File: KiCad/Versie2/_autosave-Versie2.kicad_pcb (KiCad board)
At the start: 2 copper layers, 95 parts, among them IC1 AP9221SA-CC-HAC-7, IC2 ISL91107IRTNZ-T7A, J1 Micro_SD_Card, J10 Screw_Terminal_01x02, J11 Screw_Terminal_01x02, J12 Screw_Terminal_01x03, J2 USB_C_Receptacle_USB3.0, J3 JTAG, J4 Programmer, J5 Conn_01x06_Male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

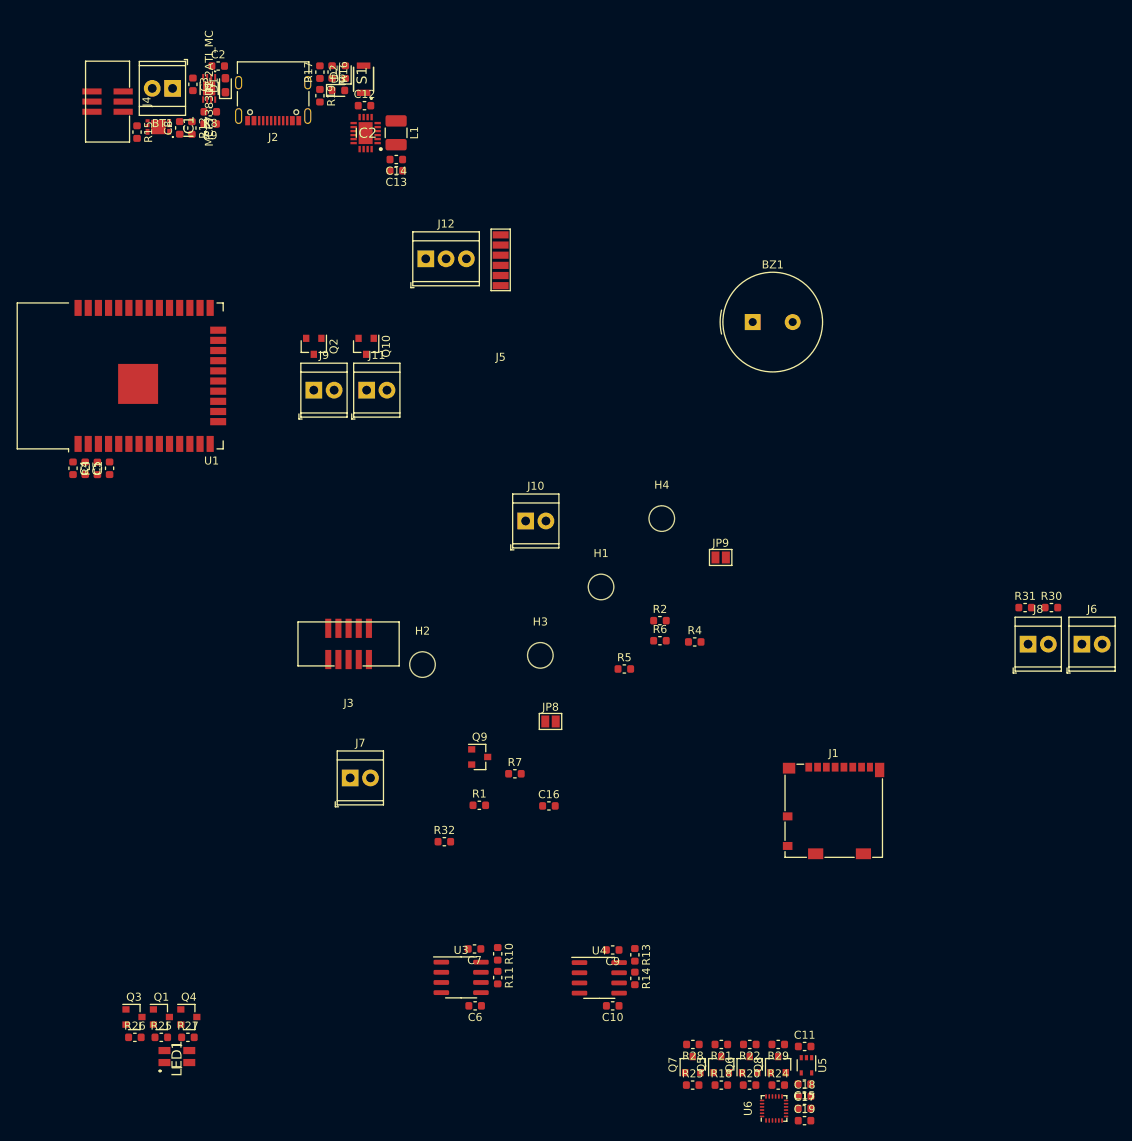
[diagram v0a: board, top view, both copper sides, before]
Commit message: KiCad Plaatsing componenten
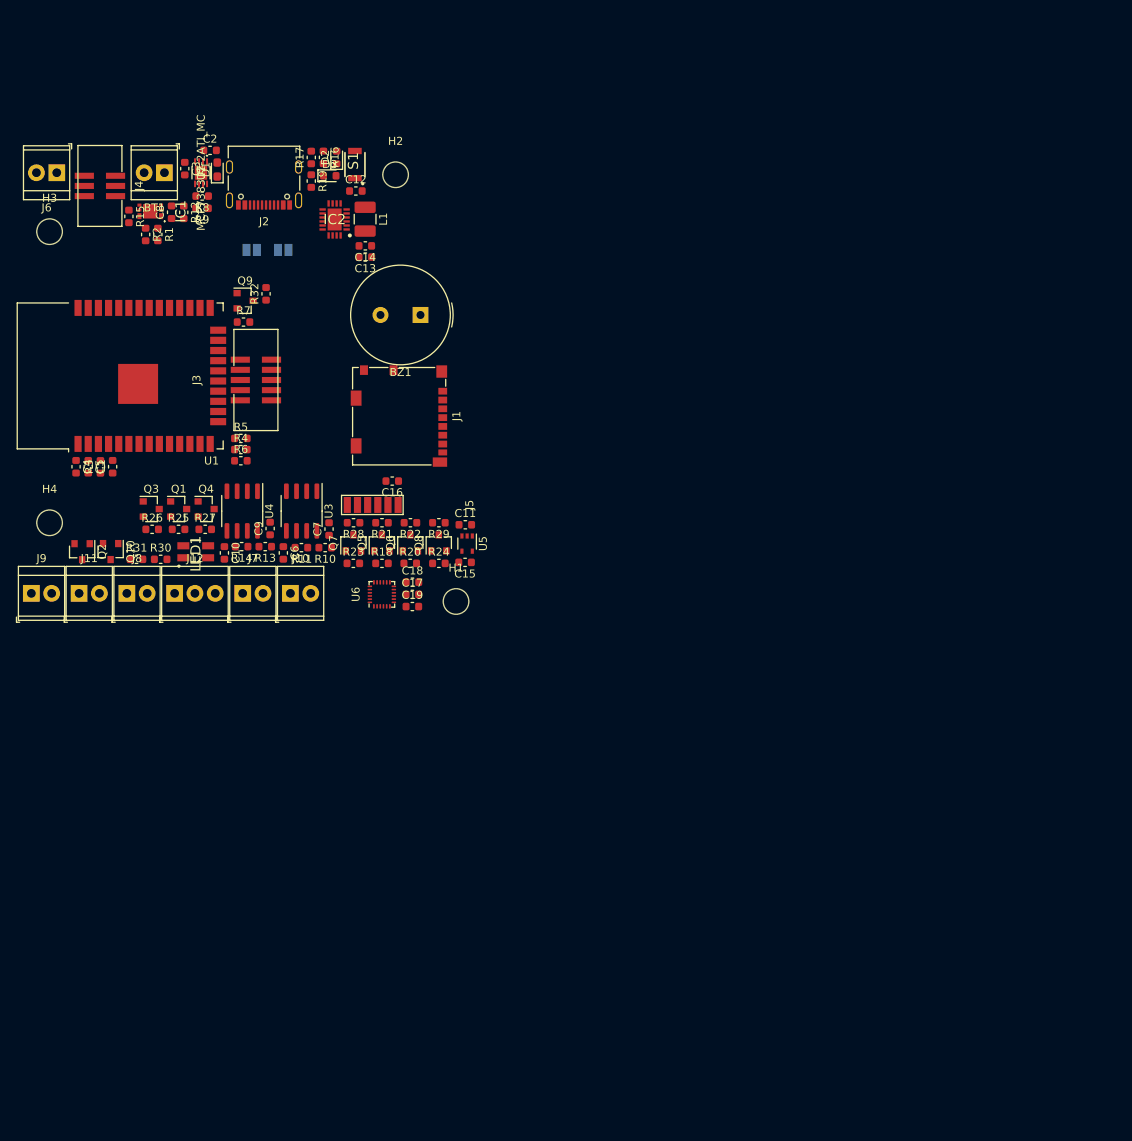
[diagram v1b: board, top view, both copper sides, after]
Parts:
- JP8, JP9: moved to B.Cu
- moved J6 141.0 mm to (64.9, 47.2), turned to 180 degrees
- moved J8 112.8 mm to (73.7, 99.8)
- moved R30 111.5 mm to (77.9, 95.6)
- moved R31 111.2 mm to (74.9, 95.6)
- moved R1 81.9 mm to (77.5, 55.0), turned to 270 degrees
- moved H3 81.0 mm to (64.0, 54.6)
- moved C17 80.8 mm to (109.3, 99.9)
- moved C18 80.8 mm to (109.4, 98.4)
- moved C19 80.8 mm to (109.3, 101.5)
- moved U6 80.8 mm to (105.5, 99.9)
- moved R2 80.4 mm to (76.0, 55.0), turned to 270 degrees
- moved Q5 77.8 mm to (105.5, 93.5)
- moved Q7 77.8 mm to (102.0, 93.5)
- moved Q8 77.8 mm to (112.6, 93.5)
- moved C11 77.8 mm to (116.0, 91.2)
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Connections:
- IC1 pad 4: Net-(IC1-Pad4) -> (no net)
- IC1 pad 7: Net-(IC1-Pad7) -> (no net)
- IC2 pad 11: Net-(IC2-Pad11) -> (no net)
- J1 pad 1: Net-(J1-Pad1) -> (no net)
- J1 pad 8: Net-(J1-Pad8) -> (no net)
- J2 pad A5: Net-(J2-PadA5) -> (no net)
- J2 pad A6: Net-(J2-PadA6) -> (no net)
- J2 pad A7: Net-(J2-PadA7) -> (no net)
- J2 pad A8: Net-(J2-PadA8) -> (no net)
- J2 pad B5: Net-(J2-PadB5) -> (no net)
- J2 pad B6: Net-(J2-PadB6) -> (no net)
- J2 pad B7: Net-(J2-PadB7) -> (no net)
- J2 pad B8: Net-(J2-PadB8) -> (no net)
- J3 pad 1: +3V3 -> (no net)
- J3 pad 6: Net-(J3-Pad6) -> (no net)
- J4 pad 6: +3V3 -> (no net)
- U1 pad 10: Green_LED -> Capacitive_Stretch2_OUT
- U1 pad 11: Yellow_LED -> Capacitive_Stretch1_OUT
- U1 pad 17: Net-(U1-Pad17) -> (no net)
- U1 pad 18: Net-(U1-Pad18) -> (no net)
- U1 pad 19: Net-(U1-Pad19) -> (no net)
- U1 pad 20: Net-(U1-Pad20) -> (no net)
- U1 pad 21: Net-(U1-Pad21) -> (no net)
- U1 pad 22: Net-(U1-Pad22) -> (no net)
- U1 pad 32: Net-(U1-Pad32) -> (no net)
- U1 pad 4: Capacitive_Stretch1_OUT -> Resistive_Stretch1
- U1 pad 5: Capacitive_Stretch2_OUT -> Resistive_Stretch2
- U1 pad 6: Resistive_Stretch2 -> Extern_Sensor
- U1 pad 8: Extern_Sensor -> Yellow_LED
- U1 pad 9: Resistive_Stretch1 -> Green_LED
- U2 pad 7: Net-(U2-Pad7) -> (no net)
- U5 pad 4: Net-(U5-Pad4) -> (no net)
- U6 pad 1: Net-(U6-Pad1) -> (no net)
- U6 pad 11: Net-(U6-Pad11) -> (no net)
- U6 pad 12: Net-(U6-Pad12) -> (no net)
- U6 pad 14: Net-(U6-Pad14) -> (no net)
- U6 pad 15: Net-(U6-Pad15) -> (no net)
- U6 pad 16: Net-(U6-Pad16) -> (no net)
- U6 pad 17: Net-(U6-Pad17) -> (no net)
- U6 pad 19: Net-(U6-Pad19) -> (no net)
- U6 pad 2: Net-(U6-Pad2) -> (no net)
- U6 pad 21: Net-(U6-Pad21) -> (no net)
- U6 pad 3: Net-(U6-Pad3) -> (no net)
- U6 pad 4: Net-(U6-Pad4) -> (no net)
- U6 pad 5: Net-(U6-Pad5) -> (no net)
- U6 pad 6: Net-(U6-Pad6) -> (no net)
- U6 pad 7: Net-(U6-Pad7) -> (no net)
